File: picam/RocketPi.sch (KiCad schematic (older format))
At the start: 25 parts, among them J1 CAN Communication, J2 Connector_Conn_01x05_Female, J3 Conn_02x20_Counter_Clockwise_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, Q1 2SC3906K, Q2 FDS4465, U1 MCP2562, U2 INA180, U3 PIC18F26K83, Y1 ECS-040-20-4X-DU

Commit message: Finish editing schematic for the PiCAM board
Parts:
- removed Q1: 2SC3906K, 2SC3906K:2SC3906KT146R, symbol Device:Q_NPN_BCE
- removed R5: 10K, Resistor_SMD:R_0805_2012Metric_Pad1.15x1.40mm_HandSolder, symbol Device:R
- added Q1: BSS138, Package_TO_SOT_SMD:SOT-23, symbol Transistor_FET:BSS138
- C4, C5: value 30pF -> 27pF
- J1: footprint (none) -> canhw_footprints:connector_Harwin_M80-5000642
- J2: footprint (none) -> canhw_footprints:PinHeader_5x2.54_SMD_90deg_952-3198-1-ND
- Q2: value FDS4465 -> AOD417; footprint (none) -> Package_TO_SOT_SMD:TO-252-2
- U1: footprint (none) -> Package_SO:SOIC-8_3.9x4.9mm_P1.27mm
- U2: footprint (none) -> Package_TO_SOT_SMD:SOT-23-5_HandSoldering
- Y1: value ECS-040-20-4X-DU -> Crystal
- renumbered C8 to C6, C6 to C7, C7 to C8, R6 to R4, R4 to R5
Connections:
- net CURRENT_SENSE: now also U3.14 (RC3); no longer U3.3 (RA1)
- net GND: now also Q1.2 (S)
- net pi_switching: now also Q1.1 (G)
- net at Q2.2 (G), R4.2: now also Q1.3 (D)
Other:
- note added: "Crystal Frequency = 12 MHz"
- note removed: "Crystal Frequency = 4 MHz"

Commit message: Complete initial PCB layout for PiCAM board
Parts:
- added D1, D3: Device_LED, LED_SMD:LED_0805_2012Metric_Pad1.15x1.40mm_HandSolder, symbol Device:LED
- added R3, R7: 330R, Resistor_SMD:R_0805_2012Metric_Pad1.15x1.40mm_HandSolder, symbol Device:R
- renumbered D1 to D2, R3 to R4, R4 to R5, R5 to R6
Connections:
- net CURRENT_SENSE: now also U3.26 (RB5); no longer U3.14 (RC3)
- net GND: now also D1.1 (K), D3.1 (K)
- net at J3.40 (Pin_40): now also R7.1
- new net: R3.2, U3.14 (RC3)
- new net: D1.2 (A), R3.1
- new net: D3.2 (A), R7.2
- no-connect marks 42 -> 40
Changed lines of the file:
@@
 Text Label 1450 2250 0    50   ~ 0
 CANL
-$Comp
-L Device:LED D1
-U 1 1 5FF28EB3
-P 7950 3000
-F 0 "D1" H 7943 2745 50  0000 C CNN
-F 1 "Device_LED" H 7943 2836 50  0000 C CNN
-F 2 "LED_SMD:LED_0805_2012Metric_Pad1.15x1.40mm_HandSolder" H 7950 3000 50  0001 C CNN
-F 3 "" H 7950 3000 50  0001 C CNN
-	1    7950 3000
-	0    -1   -1   0
-$EndComp
 Text Notes 1400 4350 0    50   ~ 0
 HIGHSPEED CAN TRANSCEIVER
@@
 $EndComp
 $Comp
-L Device:R R5
-U 1 1 603081CF
-P 7950 2700
-F 0 "R5" V 8157 2700 50  0000 C CNN
-F 1 "330R" V 8066 2700 50  0000 C CNN
-F 2 "Resistor_SMD:R_0805_2012Metric_Pad1.15x1.40mm_HandSolder" V 7880 2700 50  0001 C CNN
-F 3 "~" H 7950 2700 50  0001 C CNN
-	1    7950 2700
-	-1   0    0    1
-$EndComp
-$Comp
 L power:GND #PWR08
 U 1 1 6031A531
@@
 	1    0    0    -1
 $EndComp
-Text Label 5350 3200 2    50   ~ 0
+Text Label 7400 2300 0    50   ~ 0
 CURRENT_SENSE
 Wire Wire Line
@@
 	7450 3300 7450 3400
 $Comp
-L power:GND #PWR015
+L power:GND #PWR016
 U 1 1 60332C4F
 P 7450 3400
-F 0 "#PWR015" H 7450 3150 50  0001 C CNN
+F 0 "#PWR016" H 7450 3150 50  0001 C CNN
 F 1 "GND" H 7455 3227 50  0000 C CNN
 F 2 "" H 7450 3400 50  0001 C CNN
@@
 CAN_TX
 $Comp
-L power:+5V #PWR016
+L power:+5V #PWR017
 U 1 1 608E1AB2
 P 7500 1550
-F 0 "#PWR016" H 7500 1400 50  0001 C CNN
+F 0 "#PWR017" H 7500 1400 50  0001 C CNN
 F 1 "+5V" H 7515 1723 50  0000 C CNN
 F 2 "" H 7500 1550 50  0001 C CNN
@@
 $EndComp
 $Comp
-L power:GND #PWR018
-U 1 1 60A3E57E
-P 7950 3150
-F 0 "#PWR018" H 7950 2900 50  0001 C CNN
-F 1 "GND" H 7955 2977 50  0000 C CNN
-F 2 "" H 7950 3150 50  0001 C CNN
-F 3 "" H 7950 3150 50  0001 C CNN
-	1    7950 3150
-	1    0    0    -1
-$EndComp
-$Comp
-L power:GND #PWR019
+L power:GND #PWR020
 U 1 1 60A3EFFA
 P 8150 1800
-F 0 "#PWR019" H 8150 1550 50  0001 C CNN
+F 0 "#PWR020" H 8150 1550 50  0001 C CNN
 F 1 "GND" H 8155 1627 50  0000 C CNN
 F 2 "" H 8150 1800 50  0001 C CNN
@@
 $EndComp
 $Comp
-L Device:R R4
+L Device:R R5
 U 1 1 60A482F1
 P 6400 4450
-F 0 "R4" H 6470 4496 50  0000 L CNN
+F 0 "R5" H 6470 4496 50  0000 L CNN
 F 1 "10K" H 6470 4405 50  0000 L CNN
 F 2 "Resistor_SMD:R_0805_2012Metric_Pad1.15x1.40mm_HandSolder" V 6330 4450 50  0001 C CNN
@@
 $EndComp
 $Comp
-L power:GND #PWR014
+L power:GND #PWR015
 U 1 1 60A49D87
 P 6900 5350
-F 0 "#PWR014" H 6900 5100 50  0001 C CNN
+F 0 "#PWR015" H 6900 5100 50  0001 C CNN
 F 1 "GND" H 6905 5177 50  0000 C CNN
 F 2 "" H 6900 5350 50  0001 C CNN
@@
 	6400 4150 6700 4150
 $Comp
-L power:+5V #PWR013
+L power:+5V #PWR014
 U 1 1 60A582B0
 P 5800 4050
-F 0 "#PWR013" H 5800 3900 50  0001 C CNN
+F 0 "#PWR014" H 5800 3900 50  0001 C CNN
 F 1 "+5V" H 5815 4223 50  0000 C CNN
 F 2 "" H 5800 4050 50  0001 C CNN
@@
 	9400 1750 8700 1750
 $Comp
-L power:+3V3 #PWR020
+L power:+3V3 #PWR021
 U 1 1 60AB728F
 P 8700 1450
-F 0 "#PWR020" H 8700 1300 50  0001 C CNN
+F 0 "#PWR021" H 8700 1300 50  0001 C CNN
 F 1 "+3V3" H 8715 1623 50  0000 C CNN
 F 2 "" H 8700 1450 50  0001 C CNN
@@
 	9400 3650 8950 3650
 $Comp
-L power:GND #PWR023
+L power:GND #PWR024
 U 1 1 60ABCB2E
 P 8950 3900
-F 0 "#PWR023" H 8950 3650 50  0001 C CNN
+F 0 "#PWR024" H 8950 3650 50  0001 C CNN
 F 1 "GND" H 8955 3727 50  0000 C CNN
 F 2 "" H 8950 3900 50  0001 C CNN
@@
 Connection ~ 10800 3350
 $Comp
-L power:GND #PWR024
+L power:GND #PWR026
 U 1 1 60AFBC8F
 P 10800 3600
-F 0 "#PWR024" H 10800 3350 50  0001 C CNN
+F 0 "#PWR026" H 10800 3350 50  0001 C CNN
 F 1 "GND" H 10805 3427 50  0000 C CNN
 F 2 "" H 10800 3600 50  0001 C CNN
@@
 NoConn ~ 9900 3450
 NoConn ~ 9900 3550
-NoConn ~ 9900 3650
 NoConn ~ 9400 3250
 Text Label 10650 1200 0    50   ~ 0
@@
 	10650 1200 10650 1750
 $Comp
-L power:GND #PWR017
+L power:GND #PWR018
 U 1 1 60B51793
 P 7500 4900
-F 0 "#PWR017" H 7500 4650 50  0001 C CNN
+F 0 "#PWR018" H 7500 4650 50  0001 C CNN
 F 1 "GND" H 7505 4727 50  0000 C CNN
 F 2 "" H 7500 4900 50  0001 C CNN
@@
 Pi_Tx
 $Comp
-L power:+3V3 #PWR021
+L power:+3V3 #PWR022
 U 1 1 60B1B745
 P 8700 4900
-F 0 "#PWR021" H 8700 4750 50  0001 C CNN
+F 0 "#PWR022" H 8700 4750 50  0001 C CNN
 F 1 "+3V3" H 8715 5073 50  0000 C CNN
 F 2 "" H 8700 4900 50  0001 C CNN
@@
 $EndComp
 $Comp
-L power:+5V #PWR025
+L power:+5V #PWR027
 U 1 1 60B1F1BC
 P 10900 4900
-F 0 "#PWR025" H 10900 4750 50  0001 C CNN
+F 0 "#PWR027" H 10900 4750 50  0001 C CNN
 F 1 "+5V" H 10915 5073 50  0000 C CNN
 F 2 "" H 10900 4900 50  0001 C CNN
@@
 Pi_Rx
 $Comp
-L power:+3V3 #PWR022
+L power:+3V3 #PWR023
 U 1 1 60B27BCD
 P 8700 5800
-F 0 "#PWR022" H 8700 5650 50  0001 C CNN
+F 0 "#PWR023" H 8700 5650 50  0001 C CNN
 F 1 "+3V3" H 8715 5973 50  0000 C CNN
 F 2 "" H 8700 5800 50  0001 C CNN
@@
 $EndComp
 $Comp
-L power:+5V #PWR026
+L power:+5V #PWR028
 U 1 1 60B27BD3
 P 10900 5800
-F 0 "#PWR026" H 10900 5650 50  0001 C CNN
+F 0 "#PWR028" H 10900 5650 50  0001 C CNN
 F 1 "+5V" H 10915 5973 50  0000 C CNN
 F 2 "" H 10900 5800 50  0001 C CNN
@@
 NoConn ~ 5750 2600
 NoConn ~ 5750 3100
-NoConn ~ 7200 2300
 NoConn ~ 7200 2600
 NoConn ~ 7200 2700
@@
 NoConn ~ 7200 2800
 $Comp
-L Device:R R3
+L Device:R R4
 U 1 1 60B17ED6
 P 5500 2000
-F 0 "R3" V 5293 2000 50  0000 C CNN
+F 0 "R4" V 5293 2000 50  0000 C CNN
 F 1 "100" V 5384 2000 50  0000 C CNN
 F 2 "Resistor_SMD:R_0805_2012Metric_Pad1.15x1.40mm_HandSolder" V 5430 2000 50  0001 C CNN
@@
 $EndComp
 $Comp
-L power:GND #PWR012
+L power:GND #PWR013
 U 1 1 60B1CCAC
 P 5250 2550
-F 0 "#PWR012" H 5250 2300 50  0001 C CNN
+F 0 "#PWR013" H 5250 2300 50  0001 C CNN
 F 1 "GND" H 5255 2377 50  0000 C CNN
 F 2 "" H 5250 2550 50  0001 C CNN
@@
 Wire Wire Line
 	7200 2400 7950 2400
-Wire Wire Line
-	7950 2400 7950 2550
 NoConn ~ 7200 2500
 $Comp
@@
 NoConn ~ 5750 2200
 Wire Wire Line
-	5750 3200 5350 3200
+	7200 2300 7400 2300
+Wire Wire Line
+	7950 2400 7950 2550
+$Comp
+L power:GND #PWR019
+U 1 1 60A3E57E
+P 7950 3150
+F 0 "#PWR019" H 7950 2900 50  0001 C CNN
+F 1 "GND" H 7955 2977 50  0000 C CNN
+F 2 "" H 7950 3150 50  0001 C CNN
+F 3 "" H 7950 3150 50  0001 C CNN
+	1    7950 3150
+	1    0    0    -1
+$EndComp
+$Comp
+L Device:R R6
+U 1 1 603081CF
+P 7950 2700
+F 0 "R6" V 8157 2700 50  0000 C CNN
+F 1 "330R" V 8066 2700 50  0000 C CNN
+F 2 "Resistor_SMD:R_0805_2012Metric_Pad1.15x1.40mm_HandSolder" V 7880 2700 50  0001 C CNN
+F 3 "~" H 7950 2700 50  0001 C CNN
+	1    7950 2700
+	-1   0    0    1
+$EndComp
+$Comp
+L Device:LED D2
+U 1 1 5FF28EB3
+P 7950 3000
+F 0 "D2" H 7943 2745 50  0000 C CNN
+F 1 "Device_LED" H 7943 2836 50  0000 C CNN
+F 2 "LED_SMD:LED_0805_2012Metric_Pad1.15x1.40mm_HandSolder" H 7950 3000 50  0001 C CNN
+F 3 "" H 7950 3000 50  0001 C CNN
+	1    7950 3000
+	0    -1   -1   0
+$EndComp
+$Comp
+L power:GND #PWR012
+U 1 1 60BDB468
+P 5150 4100
+F 0 "#PWR012" H 5150 3850 50  0001 C CNN
+F 1 "GND" H 5155 3927 50  0000 C CNN
+F 2 "" H 5150 4100 50  0001 C CNN
+F 3 "" H 5150 4100 50  0001 C CNN
+	1    5150 4100
+	1    0    0    -1
+$EndComp
+$Comp
+L Device:R R3
+U 1 1 60BDB46E
+P 5150 3650
+F 0 "R3" V 5357 3650 50  0000 C CNN
+F 1 "330R" V 5266 3650 50  0000 C CNN
+F 2 "Resistor_SMD:R_0805_2012Metric_Pad1.15x1.40mm_HandSolder" V 5080 3650 50  0001 C CNN
+F 3 "~" H 5150 3650 50  0001 C CNN
+	1    5150 3650
+	-1   0    0    1
+$EndComp
+$Comp
+L Device:LED D1
+U 1 1 60BDB474
+P 5150 3950
+F 0 "D1" H 5143 3695 50  0000 C CNN
+F 1 "Device_LED" H 5143 3786 50  0000 C CNN
+F 2 "LED_SMD:LED_0805_2012Metric_Pad1.15x1.40mm_HandSolder" H 5150 3950 50  0001 C CNN
+F 3 "" H 5150 3950 50  0001 C CNN
+	1    5150 3950
+	0    -1   -1   0
+$EndComp
+Wire Wire Line
+	5150 3200 5750 3200
+Wire Wire Line
+	5150 3200 5150 3500
+Wire Wire Line
+	10400 3650 10400 3800
+$Comp
+L power:GND #PWR025
+U 1 1 60BE6913
+P 10400 4100
+F 0 "#PWR025" H 10400 3850 50  0001 C CNN
+F 1 "GND" H 10405 3927 50  0000 C CNN
+F 2 "" H 10400 4100 50  0001 C CNN
+F 3 "" H 10400 4100 50  0001 C CNN
+	1    10400 4100
+	1    0    0    -1
+$EndComp
+$Comp
+L Device:R R7
+U 1 1 60BE6919
+P 10150 3650
+F 0 "R7" V 10357 3650 50  0000 C CNN
+F 1 "330R" V 10266 3650 50  0000 C CNN
+F 2 "Resistor_SMD:R_0805_2012Metric_Pad1.15x1.40mm_HandSolder" V 10080 3650 50  0001 C CNN
+F 3 "~" H 10150 3650 50  0001 C CNN
+	1    10150 3650
+	0    -1   -1   0
+$EndComp
+$Comp
+L Device:LED D3
+U 1 1 60BE691F
+P 10400 3950
+F 0 "D3" H 10393 3695 50  0000 C CNN
+F 1 "Device_LED" H 10393 3786 50  0000 C CNN
+F 2 "LED_SMD:LED_0805_2012Metric_Pad1.15x1.40mm_HandSolder" H 10400 3950 50  0001 C CNN
+F 3 "" H 10400 3950 50  0001 C CNN
+	1    10400 3950
+	0    -1   -1   0
+$EndComp
+Wire Wire Line
+	10300 3650 10400 3650
+Wire Wire Line
+	9900 3650 10000 3650
 $EndSCHEMATC

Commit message: Fix AOD417 wiring
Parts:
- Q2: symbol Device:Q_PMOS_DGS -> Device:Q_PMOS_GDS
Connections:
- net power_pi: now also Q2.2 (D); no longer Q2.1 (D)
- net at Q1.3 (D), R5.2: now also Q2.1 (G); no longer Q2.2 (G)
- no-connect marks 40 -> 39
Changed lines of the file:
@@
 $EndComp
 $Comp
-L Device:Q_PMOS_DGS Q2
+L Device:Q_PMOS_GDS Q2
 U 1 1 60A43FDA
 P 6900 4250
@@
 	1    0    0    -1
 $EndComp
-NoConn ~ 9650 3850
 NoConn ~ 9400 3550
 NoConn ~ 9400 3450

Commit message: Add gate resistor and redo some routing
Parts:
- added R12: 50K, Resistor_SMD:R_0805_2012Metric_Pad1.15x1.40mm_HandSolder, symbol Device:R
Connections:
- net GND: now also R12.2
- net pi_switching: now also R12.1
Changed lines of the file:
@@
 pi_switching
 Wire Wire Line
-	5900 4950 6600 4950
+	5900 4950 6400 4950
 Wire Wire Line
 	9400 1750 8700 1750
@@
 Wire Wire Line
 	9900 3650 10000 3650
+$Comp
+L Device:R R12
+U 1 1 60C17605
+P 6400 5200
+F 0 "R12" H 6470 5246 50  0000 L CNN
+F 1 "50K" H 6470 5155 50  0000 L CNN
+F 2 "Resistor_SMD:R_0805_2012Metric_Pad1.15x1.40mm_HandSolder" V 6330 5200 50  0001 C CNN
+F 3 "~" H 6400 5200 50  0001 C CNN
+	1    6400 5200
+	1    0    0    -1
+$EndComp
+$Comp
+L power:GND #PWR029
+U 1 1 60C1821E
+P 6400 5450
+F 0 "#PWR029" H 6400 5200 50  0001 C CNN
+F 1 "GND" H 6405 5277 50  0000 C CNN
+F 2 "" H 6400 5450 50  0001 C CNN
+F 3 "" H 6400 5450 50  0001 C CNN
+	1    6400 5450
+	1    0    0    -1
+$EndComp
+Wire Wire Line
+	6400 5050 6400 4950
+Connection ~ 6400 4950
+Wire Wire Line
+	6400 4950 6600 4950
+Wire Wire Line
+	6400 5450 6400 5350
 $EndSCHEMATC

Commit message: Add Gerber files to the PiCAM project
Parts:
- R7: value 330R -> 600R
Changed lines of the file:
@@
 P 10150 3650
 F 0 "R7" V 10357 3650 50  0000 C CNN
-F 1 "330R" V 10266 3650 50  0000 C CNN
+F 1 "600R" V 10266 3650 50  0000 C CNN
 F 2 "Resistor_SMD:R_0805_2012Metric_Pad1.15x1.40mm_HandSolder" V 10080 3650 50  0001 C CNN
 F 3 "~" H 10150 3650 50  0001 C CNN

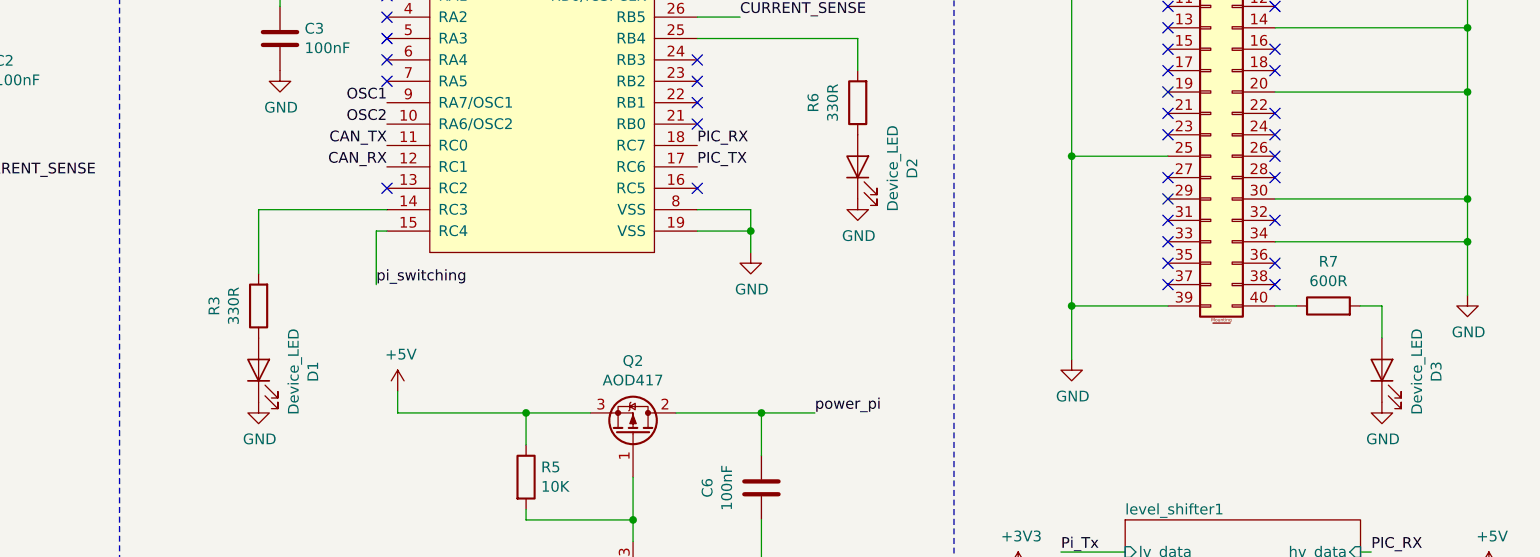
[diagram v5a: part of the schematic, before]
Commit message: Add LED colours to the picam schematic
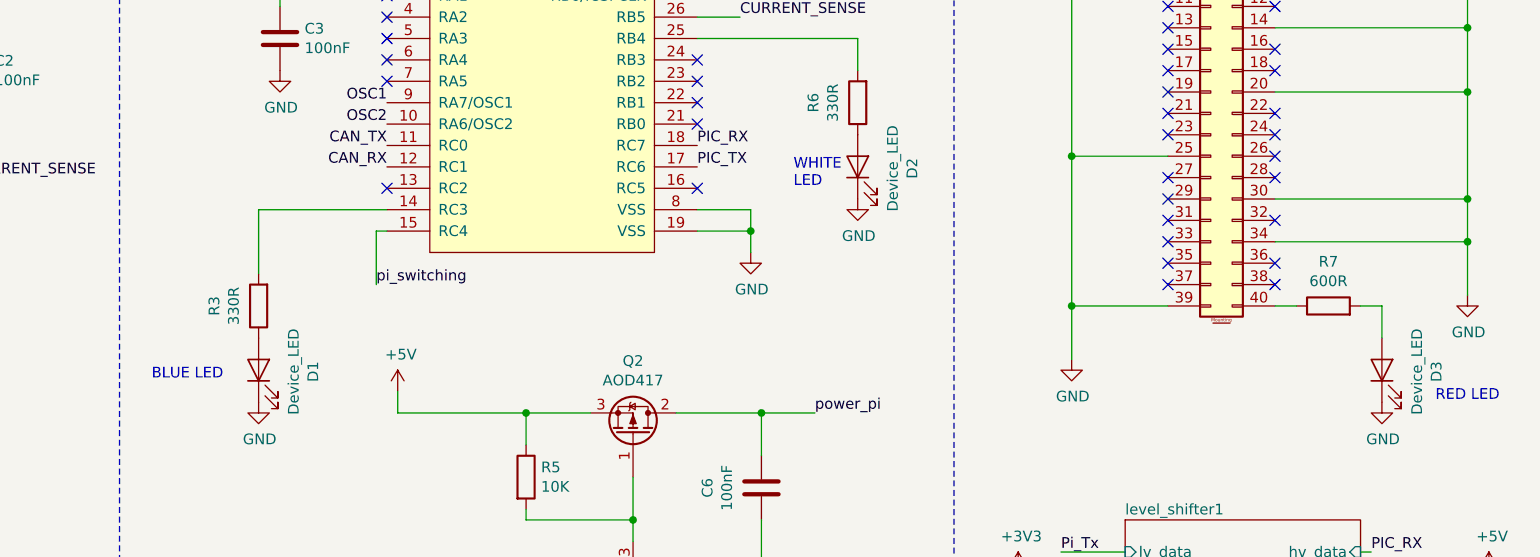
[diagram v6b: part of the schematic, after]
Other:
- note added: "BLUE LED\n"
- note added: "RED LED\n"
- note added: "WHITE\nLED"
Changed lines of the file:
@@
 Wire Wire Line
 	6400 5450 6400 5350
+Text Notes 10650 4100 0    50   ~ 0
+RED LED\n
+Text Notes 4650 4000 0    50   ~ 0
+BLUE LED\n
+Text Notes 7650 3100 0    50   ~ 0
+WHITE\nLED
 $EndSCHEMATC
